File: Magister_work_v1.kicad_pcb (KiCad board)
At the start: 2 copper layers, 100 x 100 mm, 79 parts, among them J1 Conn_01x04_Pin, J10 Conn_01x02_Pin, J2 Conn_01x03_Pin, J3 Conn_01x03_Pin, J4 Conn_01x03_Pin, J5 Conn_01x03_Pin, J6 Conn_01x04_Pin, J7 Conn_01x04_Pin, J8 Conn_01x06_Pin, J9 Conn_01x02_Pin, U1 LM66100DCK, U2 XC6206P332MR, U3 Ai-Thinker-Ra-01, U4 MCP6001-OT, Y1 X322525MQB4SI

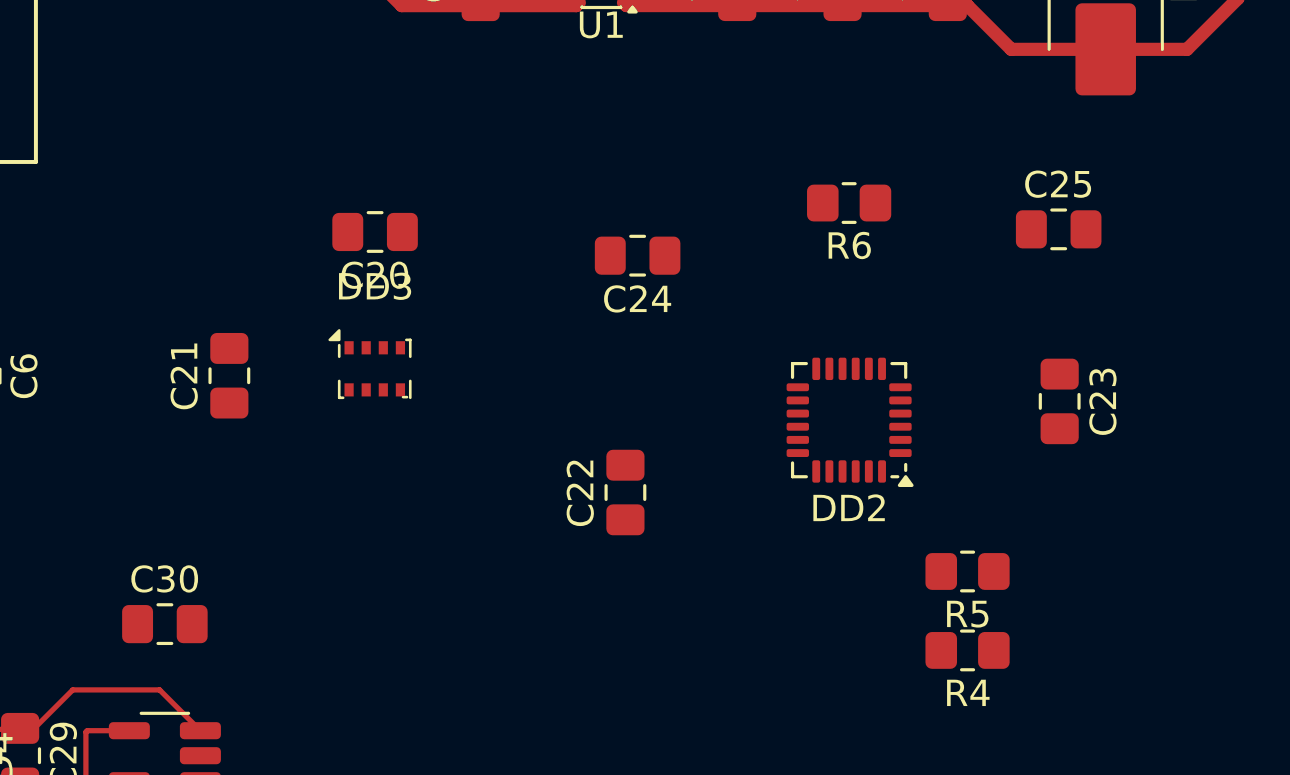
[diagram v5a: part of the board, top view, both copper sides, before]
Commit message: feat: replace MPU6050 perefery
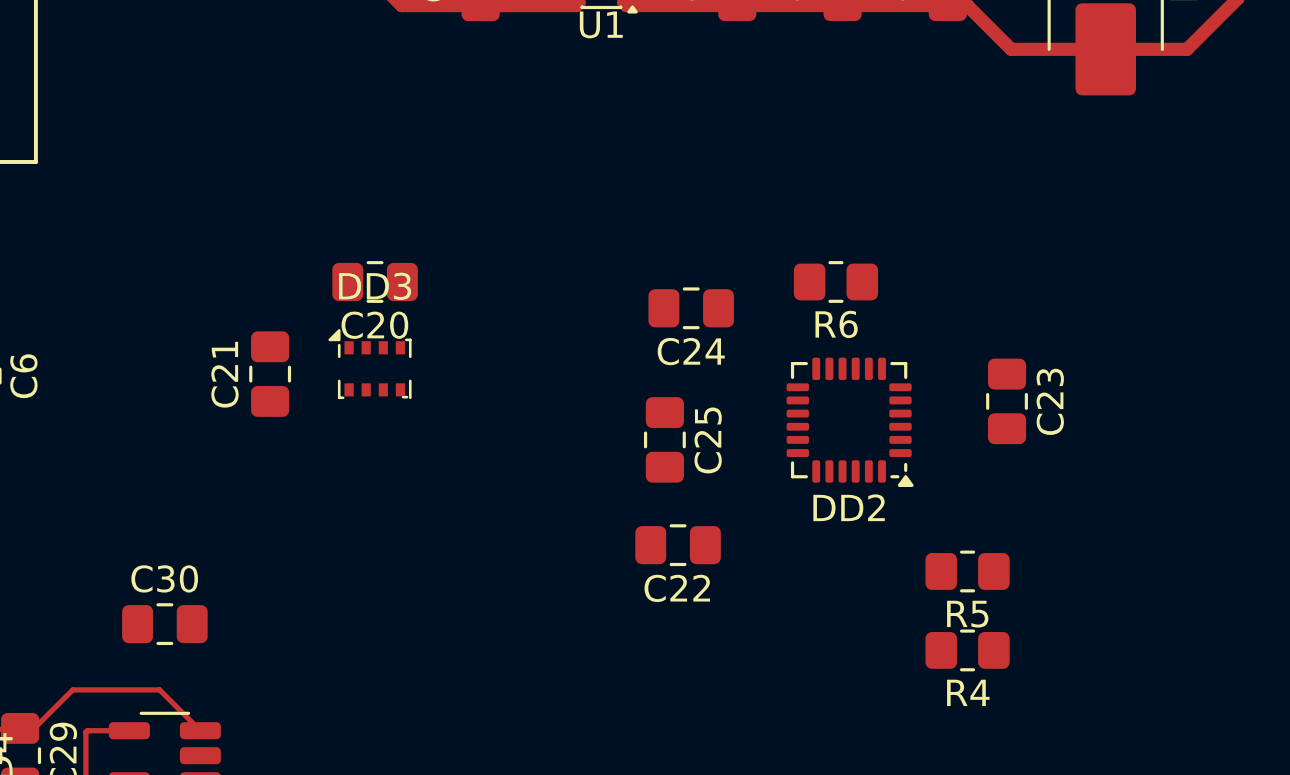
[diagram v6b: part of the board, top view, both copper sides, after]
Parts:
- moved C25 17.0 mm to (77.0, 52.5), turned to -90 degrees
- moved R6 3.04 mm to (83.5, 46.5)
- moved C24 2.86 mm to (78.0, 47.5)
- moved C22 2.83 mm to (77.5, 56.5), turned to 180 degrees
- moved C23 2.00 mm to (90.0, 51.0)
- moved C20 1.90 mm to (66.0, 46.5)
- moved C21 1.55 mm to (62.0, 50.0)
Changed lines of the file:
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@@
 		(capping no)
 		(filling no)
-		(zone_defaults)
 		(pcbplotparams
 			(layerselection 0x00000000_00000000_55555555_5755f5ff)
@@
 	(footprint "Capacitor_SMD:C_0805_2012Metric_Pad1.18x1.45mm_HandSolder"
 		(layer "F.Cu")
-		(at 91.9625 44.5)
+		(at 77 52.5 -90)
 		(descr "Capacitor SMD 0805 (2012 Metric), square (rectangular) end terminal, IPC-7351 nominal with elongated pad for handsoldering. (Body size source: IPC-SM-782 page 76, https://www.pcb-3d.com/wordpress/wp-content/uploads/ipc-sm-782a_amendment_1_and_2.pdf, https://docs.google.com/spreadsheets/d/1BsfQQcO9C6DZCsRaXUlFlo91Tg2WpOkGARC1WS5S8t0/edit?usp=sharing)")
 		(tags "capacitor handsolder")
 		(property "Reference" "C25"
-			(at 0 -1.68 0)
+			(at 0 -1.68 90)
 			(layer "F.SilkS")
 			(effects
@@
 		)
 		(property "Value" "0.1u"
-			(at 0 1.68 0)
+			(at 0 1.68 90)
 			(layer "F.Fab")
 			(effects
@@
 		)
 		(property "Datasheet" ""
-			(at 0 0 0)
+			(at 0 0 90)
 			(layer "F.Fab")
 			(hide yes)
@@
 		)
 		(property "Description" "Unpolarized capacitor, small symbol"
-			(at 0 0 0)
+			(at 0 0 90)
 			(layer "F.Fab")
 			(hide yes)
@@
 		(duplicate_pad_numbers_are_jumpers no)
 		(fp_line
-			(start -0.261252 -0.735)
-			(end 0.261252 -0.735)
+			(start -0.261252 0.735)
+			(end 0.261252 0.735)
 			(stroke
 				(width 0.12)
@@
 		)
 		(fp_line
-			(start -0.261252 0.735)
-			(end 0.261252 0.735)
+			(start -0.261252 -0.735)
+			(end 0.261252 -0.735)
 			(stroke
 				(width 0.12)
@@
 		)
 		(fp_text user "${REFERENCE}"
-			(at 0 0 0)
+			(at 0 0 90)
 			(layer "F.Fab")
 			(effects
@@
 		)
 		(pad "1" smd roundrect
-			(at -1.0375 0)
+			(at -1.0375 0 270)
 			(size 1.175 1.45)
 			(layers "F.Cu" "F.Mask" "F.Paste")
@@
 		)
 		(pad "2" smd roundrect
-			(at 1.0375 0)
+			(at 1.0375 0 270)
 			(size 1.175 1.45)
 			(layers "F.Cu" "F.Mask" "F.Paste")
@@
 	(footprint "Capacitor_SMD:C_0805_2012Metric_Pad1.18x1.45mm_HandSolder"
 		(layer "F.Cu")
-		(at 92 51.0375 -90)
+		(at 90 51.0375 -90)
 		(descr "Capacitor SMD 0805 (2012 Metric), square (rectangular) end terminal, IPC-7351 nominal with elongated pad for handsoldering. (Body size source: IPC-SM-782 page 76, https://www.pcb-3d.com/wordpress/wp-content/uploads/ipc-sm-782a_amendment_1_and_2.pdf, https://docs.google.com/spreadsheets/d/1BsfQQcO9C6DZCsRaXUlFlo91Tg2WpOkGARC1WS5S8t0/edit?usp=sharing)")
 		(tags "capacitor handsolder")
@@
 	(footprint "Capacitor_SMD:C_0805_2012Metric_Pad1.18x1.45mm_HandSolder"
 		(layer "F.Cu")
-		(at 75.9625 45.5 180)
+		(at 78 47.5 180)
 		(descr "Capacitor SMD 0805 (2012 Metric), square (rectangular) end terminal, IPC-7351 nominal with elongated pad for handsoldering. (Body size source: IPC-SM-782 page 76, https://www.pcb-3d.com/wordpress/wp-content/uploads/ipc-sm-782a_amendment_1_and_2.pdf, https://docs.google.com/spreadsheets/d/1BsfQQcO9C6DZCsRaXUlFlo91Tg2WpOkGARC1WS5S8t0/edit?usp=sharing)")
 		(tags "capacitor handsolder")
@@
 	(footprint "Resistor_SMD:R_0805_2012Metric_Pad1.20x1.40mm_HandSolder"
 		(layer "F.Cu")
-		(at 84 43.5 180)
+		(at 83.5 46.5 180)
 		(descr "Resistor SMD 0805 (2012 Metric), square (rectangular) end terminal, IPC-7351 nominal with elongated pad for handsoldering. (Body size source: IPC-SM-782 page 72, https://www.pcb-3d.com/wordpress/wp-content/uploads/ipc-sm-782a_amendment_1_and_2.pdf)")
 		(tags "resistor handsolder")
@@
 	(footprint "Capacitor_SMD:C_0805_2012Metric_Pad1.18x1.45mm_HandSolder"
 		(layer "F.Cu")
-		(at 60.45 50.0625 90)
+		(at 62 50 90)
 		(descr "Capacitor SMD 0805 (2012 Metric), square (rectangular) end terminal, IPC-7351 nominal with elongated pad for handsoldering. (Body size source: IPC-SM-782 page 76, https://www.pcb-3d.com/wordpress/wp-content/uploads/ipc-sm-782a_amendment_1_and_2.pdf, https://docs.google.com/spreadsheets/d/1BsfQQcO9C6DZCsRaXUlFlo91Tg2WpOkGARC1WS5S8t0/edit?usp=sharing)")
 		(tags "capacitor handsolder")
@@
 	(footprint "Capacitor_SMD:C_0805_2012Metric_Pad1.18x1.45mm_HandSolder"
 		(layer "F.Cu")
-		(at 65.9875 44.6 180)
+		(at 65.9875 46.5 180)
 		(descr "Capacitor SMD 0805 (2012 Metric), square (rectangular) end terminal, IPC-7351 nominal with elongated pad for handsoldering. (Body size source: IPC-SM-782 page 76, https://www.pcb-3d.com/wordpress/wp-content/uploads/ipc-sm-782a_amendment_1_and_2.pdf, https://docs.google.com/spreadsheets/d/1BsfQQcO9C6DZCsRaXUlFlo91Tg2WpOkGARC1WS5S8t0/edit?usp=sharing)")
 		(tags "capacitor handsolder")
@@
 	(footprint "Capacitor_SMD:C_0805_2012Metric_Pad1.18x1.45mm_HandSolder"
 		(layer "F.Cu")
-		(at 75.5 54.5 90)
+		(at 77.5 56.5 180)
 		(descr "Capacitor SMD 0805 (2012 Metric), square (rectangular) end terminal, IPC-7351 nominal with elongated pad for handsoldering. (Body size source: IPC-SM-782 page 76, https://www.pcb-3d.com/wordpress/wp-content/uploads/ipc-sm-782a_amendment_1_and_2.pdf, https://docs.google.com/spreadsheets/d/1BsfQQcO9C6DZCsRaXUlFlo91Tg2WpOkGARC1WS5S8t0/edit?usp=sharing)")
 		(tags "capacitor handsolder")
 		(property "Reference" "C22"
-			(at 0 -1.68 90)
+			(at 0 -1.68 0)
 			(layer "F.SilkS")
 			(effects
@@
 		)
 		(property "Value" "22n"
-			(at 0 1.68 90)
+			(at 0 1.68 0)
 			(layer "F.Fab")
 			(effects
@@
 		)
 		(property "Datasheet" ""
-			(at 0 0 90)
+			(at 0 0 0)
 			(layer "F.Fab")
 			(hide yes)
@@
 		)
 		(property "Description" "Unpolarized capacitor, small symbol"
-			(at 0 0 90)
+			(at 0 0 0)
 			(layer "F.Fab")
 			(hide yes)
@@
 		(duplicate_pad_numbers_are_jumpers no)
 		(fp_line
-			(start -0.261252 -0.735)
-			(end 0.261252 -0.735)
+			(start -0.261252 0.735)
+			(end 0.261252 0.735)
 			(stroke
 				(width 0.12)
@@
 		)
 		(fp_line
-			(start -0.261252 0.735)
-			(end 0.261252 0.735)
+			(start -0.261252 -0.735)
+			(end 0.261252 -0.735)
 			(stroke
 				(width 0.12)
@@
 		)
 		(fp_text user "${REFERENCE}"
-			(at 0 0 90)
+			(at 0 0 0)
 			(layer "F.Fab")
 			(effects
@@
 		)
 		(pad "1" smd roundrect
-			(at -1.0375 0 90)
+			(at -1.0375 0 180)
 			(size 1.175 1.45)
 			(layers "F.Cu" "F.Mask" "F.Paste")
@@
 		)
 		(pad "2" smd roundrect
-			(at 1.0375 0 90)
+			(at 1.0375 0 180)
 			(size 1.175 1.45)
 			(layers "F.Cu" "F.Mask" "F.Paste")
@@
 	)
 	(segment
+		(start 98.775 35.725)
+		(end 98.775 32.5)
+		(width 0.5)
+		(layer "F.Cu")
+		(net "+5V_2")
+	)
+	(segment
+		(start 87.75 35.9975)
+		(end 88.4975 35.9975)
+		(width 0.5)
+		(layer "F.Cu")
+		(net "+5V_2")
+	)
+	(segment
+		(start 87.75 35.9975)
+		(end 83.75 35.9975)
+		(width 0.5)
+		(layer "F.Cu")
+		(net "+5V_2")
+	)
+	(segment
+		(start 90.16 37.66)
+		(end 93.75 37.66)
+		(width 0.5)
+		(layer "F.Cu")
+		(net "+5V_2")
+	)
+	(segment
+		(start 93.75 37.66)
+		(end 96.84 37.66)
+		(width 0.5)
+		(layer "F.Cu")
+		(net "+5V_2")
+	)
+	(segment
+		(start 79.75 35.9975)
+		(end 75.5375 35.9975)
+		(width 0.5)
+		(layer "F.Cu")
+		(net "+5V_2")
+	)
+	(segment
+		(start 88.4975 35.9975)
+		(end 90.16 37.66)
+		(width 0.5)
+		(layer "F.Cu")
+		(net "+5V_2")
+	)
+	(segment
+		(start 83.75 35.9975)
+		(end 79.75 35.9975)
+		(width 0.5)
+		(layer "F.Cu")
+		(net "+5V_2")
+	)
+	(segment
+		(start 96.84 37.66)
+		(end 98.775 35.725)
+		(width 0.5)
+		(layer "F.Cu")
+		(net "+5V_2")
+	)
+	(segment
+		(start 75.5375 35.9975)
+		(end 75.425 35.885)
+		(width 0.5)
+		(layer "F.Cu")
+		(net "+5V_2")
+	)
+	(segment
 		(start 87.75 33.9225)
 		(end 88.5775 33.9225)
@@
 	)
 	(segment
+		(start 42.5 63.5)
+		(end 44 63.5)
+		(width 0.2)
+		(layer "F.Cu")
+		(net "Net-(R10-Pad1)")
+	)
+	(segment
+		(start 42 63)
+		(end 42.5 63.5)
+		(width 0.2)
+		(layer "F.Cu")
+		(net "Net-(R10-Pad1)")
+	)
+	(segment
+		(start 41.5 63)
+		(end 42 63)
+		(width 0.2)
+		(layer "F.Cu")
+		(net "Net-(R10-Pad1)")
+	)
+	(segment
+		(start 43.5 63)
+		(end 44 63.5)
+		(width 0.2)
+		(layer "F.Cu")
+		(net "Net-(R10-Pad1)")
+	)
+	(segment
+		(start 41.5 63)
+		(end 41.5 65.5)
+		(width 0.2)
+		(layer "F.Cu")
+		(net "Net-(R10-Pad1)")
+	)
+	(segment
 		(start 52.4625 63.5)
 		(end 52.5 63.4625)
@@
 		(net "Net-(J1-Pin_1)")
 	)
-	(segment
-		(start 98.775 35.725)
-		(end 98.775 32.5)
-		(width 0.5)
-		(layer "F.Cu")
-		(net "+5V_2")
-	)
-	(segment
-		(start 87.75 35.9975)
-		(end 88.4975 35.9975)
-		(width 0.5)
-		(layer "F.Cu")
-		(net "+5V_2")
-	)
-	(segment
-		(start 87.75 35.9975)
-		(end 83.75 35.9975)
-		(width 0.5)
-		(layer "F.Cu")
-		(net "+5V_2")
-	)
-	(segment
-		(start 90.16 37.66)
-		(end 93.75 37.66)
-		(width 0.5)
-		(layer "F.Cu")
-		(net "+5V_2")
-	)
-	(segment
-		(start 93.75 37.66)
-		(end 96.84 37.66)
-		(width 0.5)
-		(layer "F.Cu")
-		(net "+5V_2")
-	)
-	(segment
-		(start 79.75 35.9975)
-		(end 75.5375 35.9975)
-		(width 0.5)
-		(layer "F.Cu")
-		(net "+5V_2")
-	)
-	(segment
-		(start 88.4975 35.9975)
-		(end 90.16 37.66)
-		(width 0.5)
-		(layer "F.Cu")
-		(net "+5V_2")
-	)
-	(segment
-		(start 83.75 35.9975)
-		(end 79.75 35.9975)
-		(width 0.5)
-		(layer "F.Cu")
-		(net "+5V_2")
-	)
-	(segment
-		(start 96.84 37.66)
-		(end 98.775 35.725)
-		(width 0.5)
-		(layer "F.Cu")
-		(net "+5V_2")
-	)
-	(segment
-		(start 75.5375 35.9975)
-		(end 75.425 35.885)
-		(width 0.5)
-		(layer "F.Cu")
-		(net "+5V_2")
-	)
-	(segment
-		(start 42.5 63.5)
-		(end 44 63.5)
-		(width 0.2)
-		(layer "F.Cu")
-		(net "Net-(R10-Pad1)")
-	)
-	(segment
-		(start 42 63)
-		(end 42.5 63.5)
-		(width 0.2)
-		(layer "F.Cu")
-		(net "Net-(R10-Pad1)")
-	)
-	(segment
-		(start 41.5 63)
-		(end 42 63)
-		(width 0.2)
-		(layer "F.Cu")
-		(net "Net-(R10-Pad1)")
-	)
-	(segment
-		(start 43.5 63)
-		(end 44 63.5)
-		(width 0.2)
-		(layer "F.Cu")
-		(net "Net-(R10-Pad1)")
-	)
-	(segment
-		(start 41.5 63)
-		(end 41.5 65.5)
-		(width 0.2)
-		(layer "F.Cu")
-		(net "Net-(R10-Pad1)")
-	)
 	(embedded_fonts no)

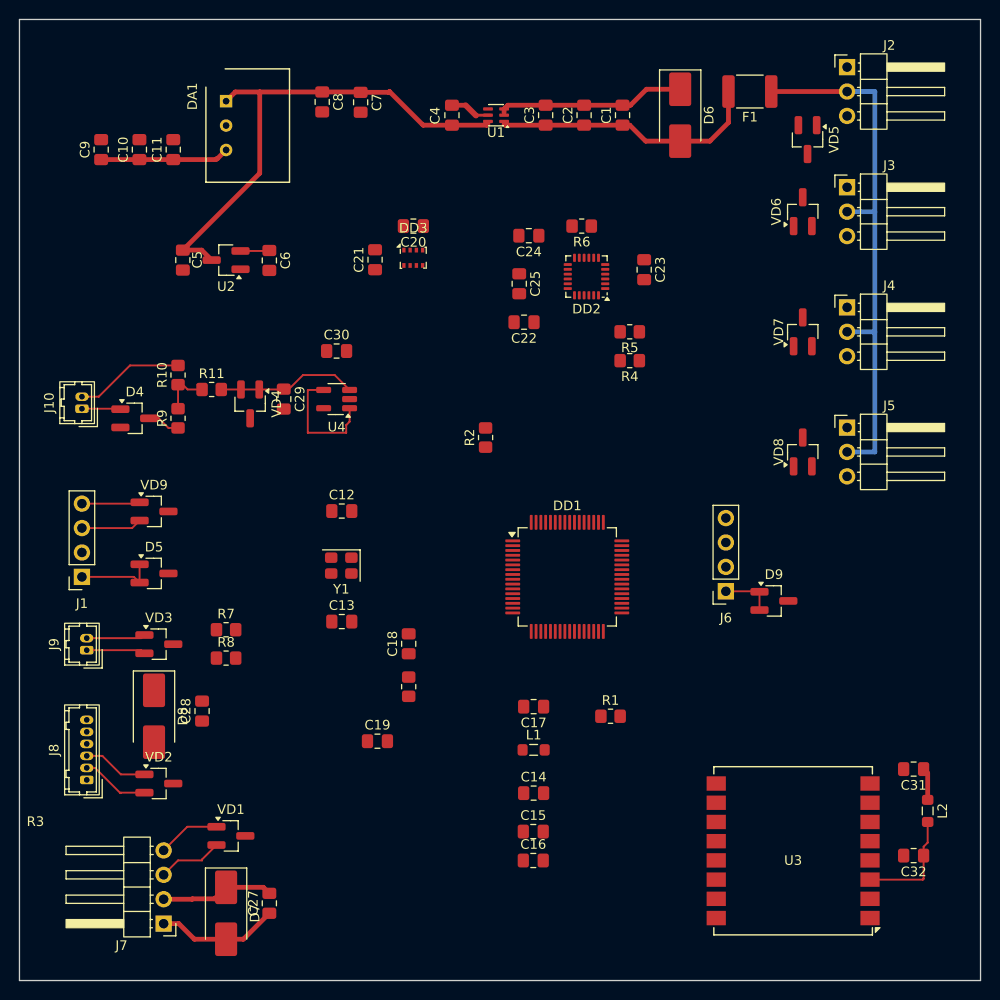
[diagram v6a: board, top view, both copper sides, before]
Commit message: feat: added line for 5V power
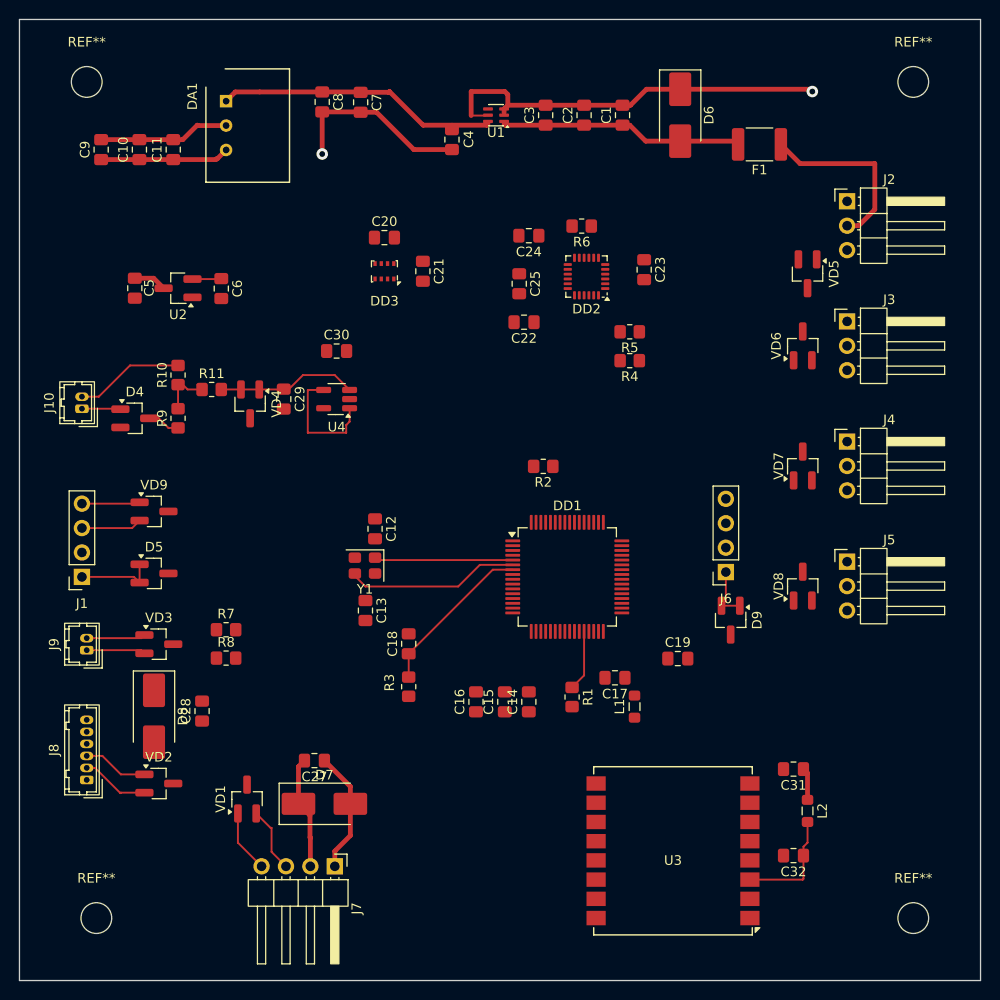
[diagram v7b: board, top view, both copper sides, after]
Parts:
- added REF**: MountingHole_3.2mm_M3, MountingHole:MountingHole_3.2mm_M3, F.Cu at (32.0, 31.5)
- added REF**: MountingHole_3.2mm_M3, MountingHole:MountingHole_3.2mm_M3, F.Cu at (33.0, 118.5)
- added REF**: MountingHole_3.2mm_M3, MountingHole:MountingHole_3.2mm_M3, F.Cu at (118.0, 31.5)
- added REF**: MountingHole_3.2mm_M3, MountingHole:MountingHole_3.2mm_M3, F.Cu at (118.0, 118.5)
- moved C19 32.4 mm to (93.5, 91.5)
- moved J7 18.8 mm to (57.8, 113.1), turned to -90 degrees
- moved C16 17.6 mm to (72.5, 96.0), turned to 90 degrees
- moved C27 15.6 mm to (55.7, 102.1), turned to 180 degrees
- moved D7 15.3 mm to (56.7, 106.6), turned to 0 degrees
- moved J5 14.0 mm to (111.1, 81.4)
- moved J2 14.0 mm to (111.1, 43.9)
- moved J3 14.0 mm to (111.1, 56.4)
- moved J4 14.0 mm to (111.1, 68.9)
- moved VD5 14.0 mm to (107.0, 51.5)
- moved VD6 14.0 mm to (106.5, 59.0)
- moved VD7 14.0 mm to (106.5, 71.5)
- moved VD8 14.0 mm to (106.5, 84.0)
- moved C15 13.8 mm to (75.5, 96.0), turned to 90 degrees
- moved C31 12.5 mm to (105.5, 103.0)
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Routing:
- net GND: track 47.1 -> 173.8 mm, vias 0 -> 2
- net +5V: track 65.2 -> 45.4 mm
- net Net-(DD1-PH1): track 0.00 -> 18.1 mm
- net Net-(DD1-NRST): track 0.00 -> 16.9 mm
- net Net-(DD1-PH0): track 0.00 -> 14.4 mm
- net +5V_1: track 56.9 -> 68.4 mm
- net Net-(DD1-PB2): track 0.00 -> 6.34 mm
- net +5V_2: track 28.1 -> 25.2 mm
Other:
- copper layers 2 -> 4
